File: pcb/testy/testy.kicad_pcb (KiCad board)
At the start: 2 copper layers, 116.4 x 88.4 mm, 21 parts, among them SW0:0 SW_Push, SW0:1 SW_Push, SW0:2 SW_Push, SW1:0 SW_Push, SW1:1 SW_Push, SW1:2 SW_Push, U1 ProMicro

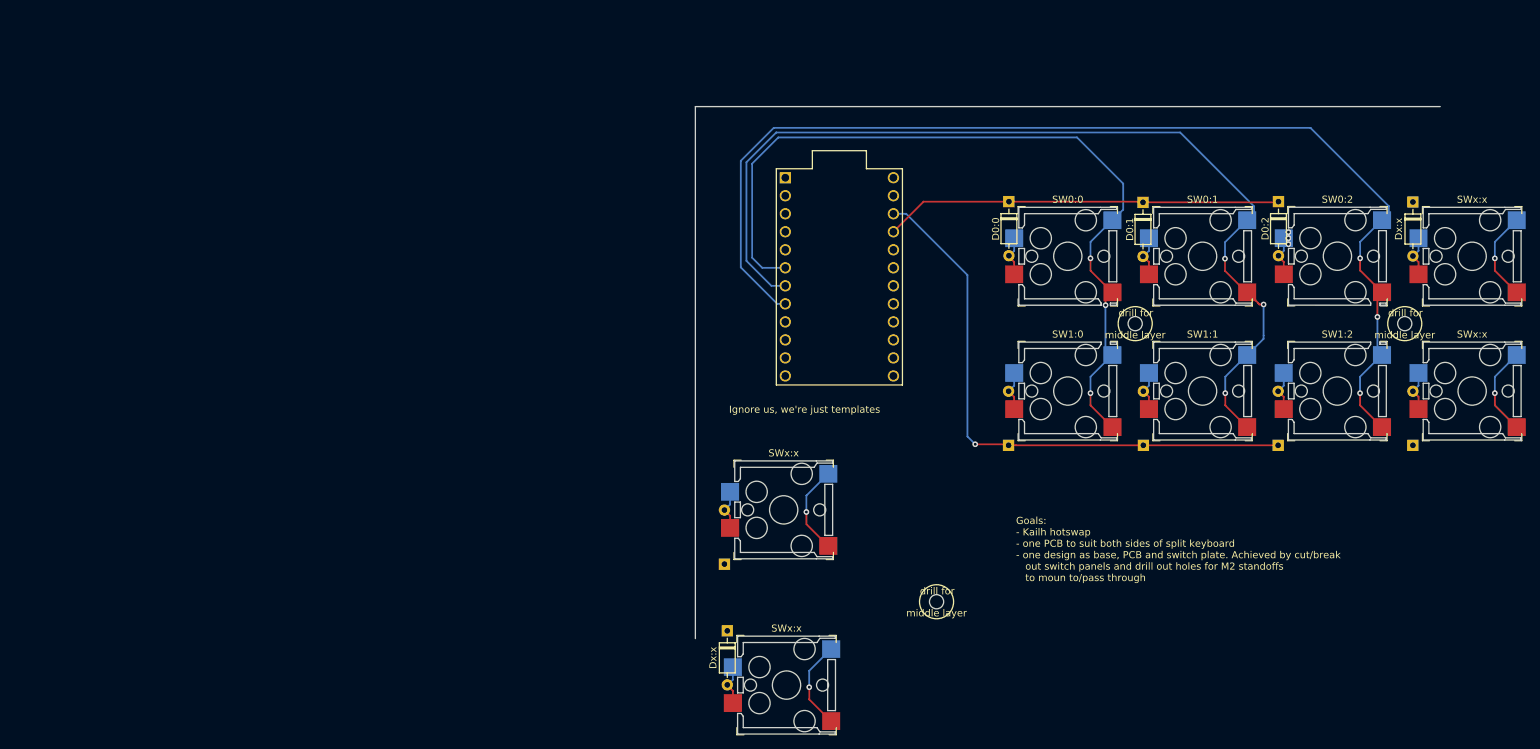
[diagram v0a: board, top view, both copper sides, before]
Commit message: feat: add reset switch and TRRS connector, test making promicro snapoff
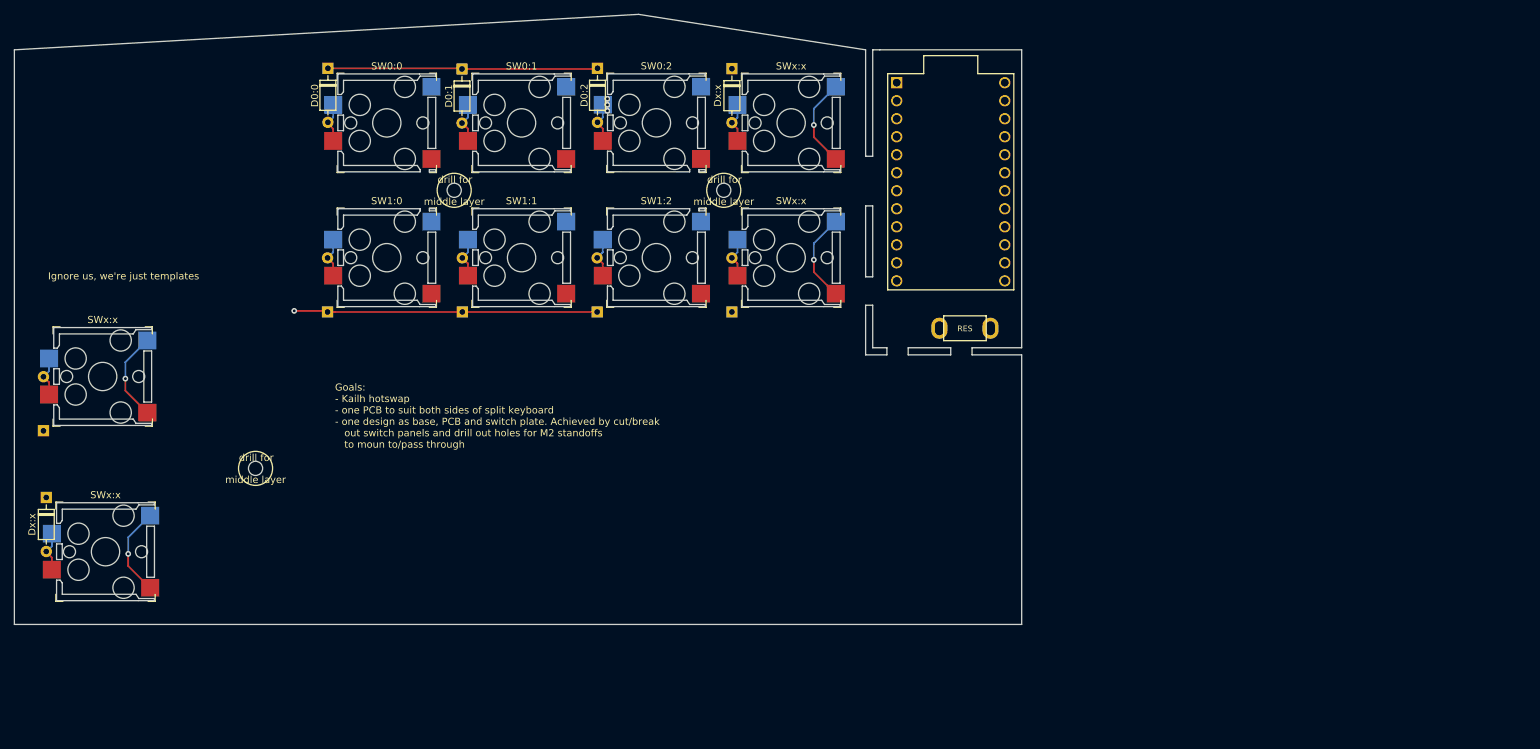
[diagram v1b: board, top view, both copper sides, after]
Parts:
- added RES1: SW_PUSH, footprints:TACT_SWITCH_TVBP06, F.Cu at (188.0, 83.0)
- moved D0:1 97.8 mm to (117.1, 44.7)
- moved D0:2 97.8 mm to (136.2, 44.6)
- moved D1:0 97.8 mm to (98.2, 79.0)
- moved D1:1 97.8 mm to (117.2, 79.0)
- moved D1:2 97.8 mm to (136.2, 79.0)
- moved Dx:x 97.8 mm to (155.2, 44.6)
- moved Dx:x 97.8 mm to (155.2, 79.0)
- moved Dx:x 97.8 mm to (58.5, 105.1)
- moved Dx:x 97.8 mm to (58.1, 95.7)
- moved SW0:0 97.8 mm to (106.5, 52.3)
- moved SW0:1 97.8 mm to (125.5, 52.3)
- moved SW0:2 97.8 mm to (144.5, 52.3)
- moved SW1:0 97.8 mm to (106.5, 71.3)
- moved SW1:1 97.8 mm to (125.5, 71.3)
- moved SW1:2 97.8 mm to (144.5, 71.3)
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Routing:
- net Col2: track 158.5 -> 0.00 mm, vias 3 -> 0
- net Col1: track 137.4 -> 0.00 mm, vias 3 -> 0
- net Col0: track 116.0 -> 0.00 mm, vias 3 -> 0
- net Row1: track 81.1 -> 42.8 mm
- net Row0: track 56.1 -> 38.1 mm
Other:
- board size 116.4 x 88.4 mm -> 142 x 86 mm

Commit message: feat: add all switches and LEDs to schematic
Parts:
- added Drill: MountingHole_2.2mm_M2_Pad_Via, MountingHole:MountingHole_2.2mm_M2_Pad_Via, F.Cu at (116.0, 61.8)
- added Drill: MountingHole_2.2mm_M2_Pad_Via, MountingHole:MountingHole_2.2mm_M2_Pad_Via, F.Cu at (154.0, 61.8)
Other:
- outline, holes or cut-outs redrawn
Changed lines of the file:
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@@
   (general
     (thickness 1.6)
-    (drawings 334)
+    (drawings 326)
     (tracks 81)
     (zones 0)
-    (modules 22)
+    (modules 24)
     (nets 31)
   )
@@
     (add_net Row1)
   )
+  (module MountingHole:MountingHole_2.2mm_M2_Pad_Via (layer F.Cu)
+    (at 116 61.8 270)
+    (descr "Mounting Hole 2.2mm, M2")
+    (tags "mounting hole 2.2mm m2")
+    (attr virtual)
+    (fp_text reference Drill (at 0 -3.2 90) (layer F.SilkS)
+      (effects (font (size 1 1) (thickness 0.15)))
+    )
+    (fp_text value MountingHole_2.2mm_M2_Pad_Via (at 0 3.2 90) (layer F.Fab)
+      (effects (font (size 1 1) (thickness 0.15)))
+    )
+    (fp_text user %R (at 0.3 0 90) (layer F.Fab)
+      (effects (font (size 1 1) (thickness 0.15)))
+    )
+    (fp_circle (center 0 0) (end 2.2 0) (layer Cmts.User) (width 0.15))
+    (fp_circle (center 0 0) (end 2.45 0) (layer F.CrtYd) (width 0.05))
+    (pad 1 thru_hole circle (at 0 0 270) (size 4.4 4.4) (drill 2.2) (layers *.Cu *.Mask))
+    (pad 1 thru_hole circle (at 1.65 0 270) (size 0.7 0.7) (drill 0.4) (layers *.Cu *.Mask))
+    (pad 1 thru_hole circle (at 1.166726 1.166726 270) (size 0.7 0.7) (drill 0.4) (layers *.Cu *.Mask))
+    (pad 1 thru_hole circle (at 0 1.65 270) (size 0.7 0.7) (drill 0.4) (layers *.Cu *.Mask))
+    (pad 1 thru_hole circle (at -1.166726 1.166726 270) (size 0.7 0.7) (drill 0.4) (layers *.Cu *.Mask))
+    (pad 1 thru_hole circle (at -1.65 0 270) (size 0.7 0.7) (drill 0.4) (layers *.Cu *.Mask))
+    (pad 1 thru_hole circle (at -1.166726 -1.166726 270) (size 0.7 0.7) (drill 0.4) (layers *.Cu *.Mask))
+    (pad 1 thru_hole circle (at 0 -1.65 270) (size 0.7 0.7) (drill 0.4) (layers *.Cu *.Mask))
+    (pad 1 thru_hole circle (at 1.166726 -1.166726 270) (size 0.7 0.7) (drill 0.4) (layers *.Cu *.Mask))
+  )
+  (module MountingHole:MountingHole_2.2mm_M2_Pad_Via (layer F.Cu)
+    (at 154 61.8 270)
+    (descr "Mounting Hole 2.2mm, M2")
+    (tags "mounting hole 2.2mm m2")
+    (attr virtual)
+    (fp_text reference Drill (at 0 -3.2 90) (layer F.SilkS)
+      (effects (font (size 1 1) (thickness 0.15)))
+    )
+    (fp_text value MountingHole_2.2mm_M2_Pad_Via (at 0 3.2 90) (layer F.Fab)
+      (effects (font (size 1 1) (thickness 0.15)))
+    )
+    (fp_circle (center 0 0) (end 2.45 0) (layer F.CrtYd) (width 0.05))
+    (fp_circle (center 0 0) (end 2.2 0) (layer Cmts.User) (width 0.15))
+    (fp_text user %R (at 0.3 0 90) (layer F.Fab)
+      (effects (font (size 1 1) (thickness 0.15)))
+    )
+    (pad 1 thru_hole circle (at 1.166726 -1.166726 270) (size 0.7 0.7) (drill 0.4) (layers *.Cu *.Mask))
+    (pad 1 thru_hole circle (at 0 -1.65 270) (size 0.7 0.7) (drill 0.4) (layers *.Cu *.Mask))
+    (pad 1 thru_hole circle (at -1.166726 -1.166726 270) (size 0.7 0.7) (drill 0.4) (layers *.Cu *.Mask))
+    (pad 1 thru_hole circle (at -1.65 0 270) (size 0.7 0.7) (drill 0.4) (layers *.Cu *.Mask))
+    (pad 1 thru_hole circle (at -1.166726 1.166726 270) (size 0.7 0.7) (drill 0.4) (layers *.Cu *.Mask))
+    (pad 1 thru_hole circle (at 0 1.65 270) (size 0.7 0.7) (drill 0.4) (layers *.Cu *.Mask))
+    (pad 1 thru_hole circle (at 1.166726 1.166726 270) (size 0.7 0.7) (drill 0.4) (layers *.Cu *.Mask))
+    (pad 1 thru_hole circle (at 1.65 0 270) (size 0.7 0.7) (drill 0.4) (layers *.Cu *.Mask))
+    (pad 1 thru_hole circle (at 0 0 270) (size 4.4 4.4) (drill 2.2) (layers *.Cu *.Mask))
+  )
   (module footprints:TACT_SWITCH_TVBP06 (layer F.Cu)
     (at 188 83)
@@
   (gr_line (start 176 42) (end 196 42) (layer Edge.Cuts) (width 0.05))
   (gr_line (start 174 42) (end 174 57) (layer Edge.Cuts) (width 0.05))
-  (gr_circle (center 154 61.8) (end 155 61.8) (layer Edge.Cuts) (width 0.05))
-  (gr_text "drill for" (at 154.1 60.3) (layer F.SilkS)
-    (effects (font (size 1 1) (thickness 0.15)))
-  )
-  (gr_text "middle layer" (at 154 63.4) (layer F.SilkS)
-    (effects (font (size 1 1) (thickness 0.15)))
-  )
-  (gr_circle (center 154 61.8) (end 156.4 61.8) (layer F.SilkS) (width 0.12))
   (gr_line (start 149.2 64.7) (end 149.2 64.4) (layer Edge.Cuts) (width 0.05))
   (gr_line (start 150.5 64.7) (end 151.4 64.7) (layer Edge.Cuts) (width 0.05))
@@
   (gr_line (start 112.5 64.7) (end 112.5 64.4) (layer Edge.Cuts) (width 0.05))
   (gr_line (start 113.4 64.7) (end 112.5 64.7) (layer Edge.Cuts) (width 0.05))
-  (gr_circle (center 116 61.8) (end 118.4 61.8) (layer F.SilkS) (width 0.12))
-  (gr_circle (center 116 61.8) (end 117 61.8) (layer Edge.Cuts) (width 0.05))
-  (gr_text "drill for" (at 116.1 60.3) (layer F.SilkS)
-    (effects (font (size 1 1) (thickness 0.15)))
-  )
-  (gr_text "middle layer" (at 116 63.4) (layer F.SilkS)
-    (effects (font (size 1 1) (thickness 0.15)))
-  )
   (gr_text "Goals:\n- Kailh hotswap\n- one PCB to suit both sides of split keyboard\n- one design as base, PCB and switch plate. Achieved by cut/break\n   out switch panels and drill out holes for M2 standoffs\n   to moun to/pass through" (at 99.2 93.6) (layer F.SilkS)
     (effects (font (size 1 1) (thickness 0.15)) (justify left))

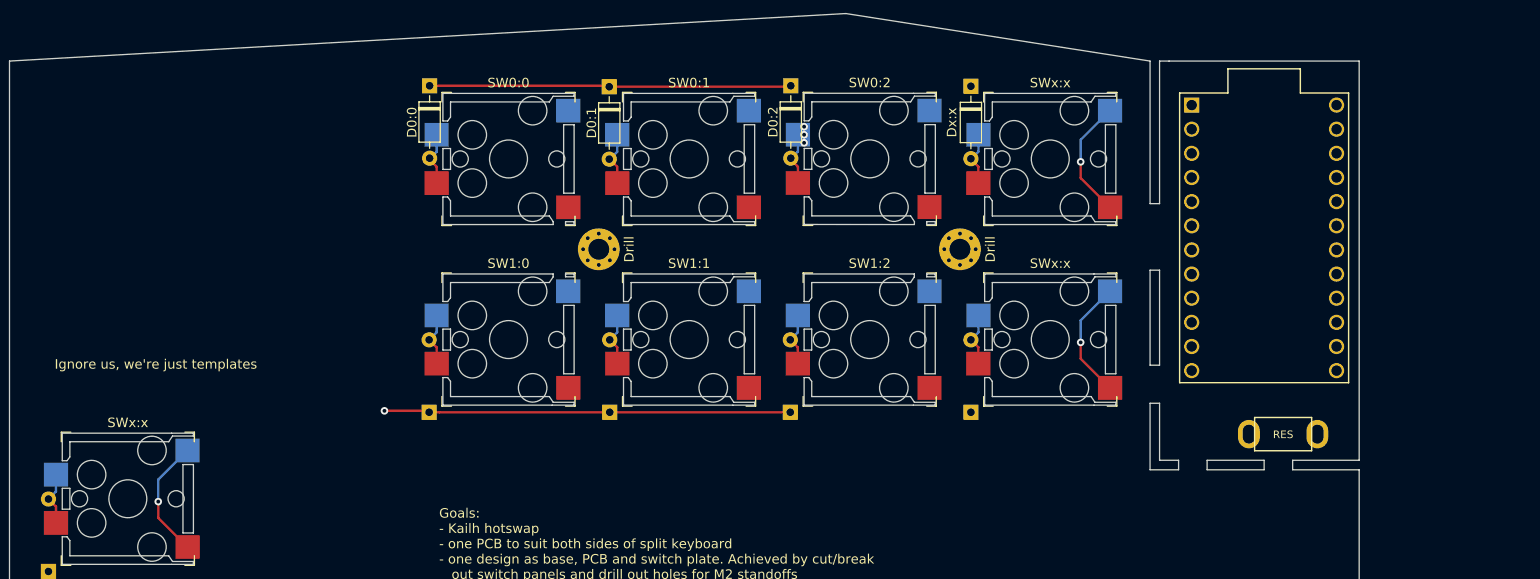
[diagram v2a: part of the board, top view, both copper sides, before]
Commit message: fix: get TRRS schematic to line up with footprint
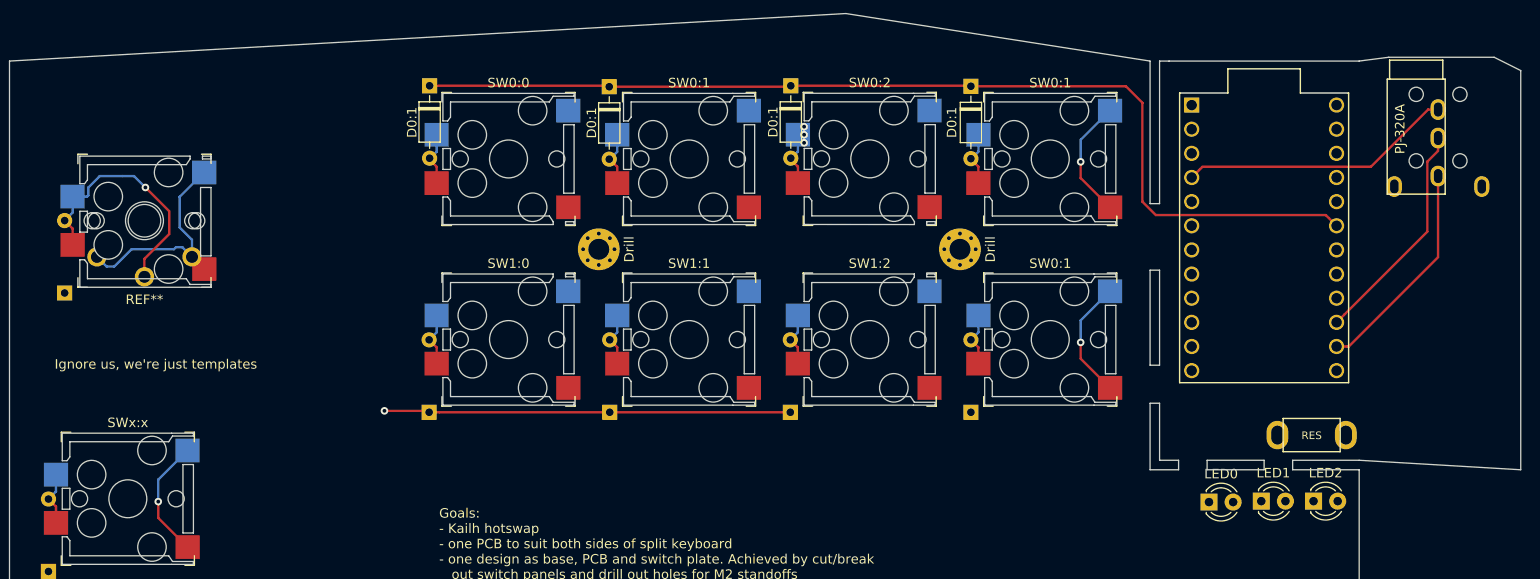
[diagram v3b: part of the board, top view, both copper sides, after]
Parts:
- removed RES1: SW_PUSH, footprints:TACT_SWITCH_TVBP06
- added Dx:x: 1N4148, Diode_THT:D_DO-35_SOD27_P7.62mm_Horizontal, B.Cu at (59.8, 66.4)
- added LED0: LED, footprints:LED_D3.0mm, F.Cu at (180.2, 88.4)
- added LED1: LED, LED_THT:LED_D3.0mm, F.Cu at (185.7, 88.3)
- added LED2: LED, LED_THT:LED_D3.0mm, F.Cu at (191.2, 88.3)
- added REF**: PG1511_socket, footprints:kailh-socket-and-choc-solder-reversible, F.Cu at (68.2, 58.8)
- added SW-reset1: SW_Push, footprints:TACT_SWITCH_TVBP06, F.Cu at (191.0, 83.1)
- added TRRS1: MJ-4PP-9, footprints:TRRS-PJ-320A-dual, F.Cu at (204.3, 43.9)
- renumbered Dx:x to D0:1, D1:2 to D0:1, D1:1 to D0:1, D1:0 to D0:1, D0:0 to D0:1, D0:2 to D0:1, SWx:x to SW0:1
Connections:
- net Net-(U1-Pad10) renamed Col5
- net Net-(U1-Pad11) renamed Col6
- net Net-(U1-Pad23) renamed Row4
- net Net-(U1-Pad9) renamed Col4
- D0:1 pad 1: (no net) -> Row0 (x2)
- D0:1 pad 2: (no net) -> Net-(D0:1-Pad2) (x2)
- D0:1 pad 1: Row1 -> Row0 (x3)
- D0:1 pad 2: Net-(D1:2-Pad2) -> Net-(D0:1-Pad2)
- D0:1 pad 2: Net-(D1:1-Pad2) -> Net-(D0:1-Pad2)
- D0:1 pad 2: Net-(D1:0-Pad2) -> Net-(D0:1-Pad2)
- D0:1 pad 2: Net-(D0:0-Pad2) -> Net-(D0:1-Pad2)
- D0:1 pad 2: Net-(D0:2-Pad2) -> Net-(D0:1-Pad2)
- SW0:1 pad 1: (no net) -> Col1 (x2)
- SW0:1 pad 2: (no net) -> Net-(D0:1-Pad2) (x2)
- U1 pad 12: Net-(U1-Pad12) -> LED2
- U1 pad 14: Net-(U1-Pad14) -> data
- U1 pad 15: Net-(U1-Pad15) -> GND
- U1 pad 16: Net-(U1-Pad16) -> GND
- U1 pad 18: Net-(U1-Pad18) -> LED0
- U1 pad 19: Net-(U1-Pad19) -> Row0
- U1 pad 2: Net-(U1-Pad2) -> GND
- U1 pad 20: Net-(U1-Pad20) -> Row1
- U1 pad 21: Row0 -> Row2
- U1 pad 22: Row1 -> Row3
- U1 pad 24: Net-(U1-Pad24) -> LED1
- U1 pad 3: Net-(U1-Pad3) -> Reset
- U1 pad 4: Net-(U1-Pad4) -> VCC
- U1 pad 5: Net-(U1-Pad5) -> Col0
- U1 pad 6: Col0 -> Col1
- U1 pad 7: Col1 -> Col2
- U1 pad 8: Col2 -> Col3
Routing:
- net Row0: track 38.1 -> 150.5 mm, vias 0 -> 1
- net Row1: track 42.8 -> 0.00 mm, vias 1 -> 0
- net VCC: track 0.00 -> 28.9 mm
- net Col1: track 0.00 -> 25.5 mm, vias 0 -> 2
- net GND: track 0.00 -> 23.8 mm
- net data: track 0.00 -> 23.1 mm
- net (no net): track 73.9 -> 87.7 mm, vias 4 -> 3
- net Net-(D0:1-Pad2): track 5.73 -> 17.2 mm
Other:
- board size 142 x 86 mm -> 159 x 86 mm

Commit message: feat: more playing with layout
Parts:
- added Dx:x: 1N4148, Diode_THT:D_DO-35_SOD27_P7.62mm_Horizontal, B.Cu at (155.2, 41.0)
- added Dx:x: 1N4148, Diode_THT:D_DO-35_SOD27_P7.62mm_Horizontal, F.Cu at (189.2, 101.7)
- added Dx:x: 1N4148, Diode_THT:D_DO-35_SOD27_P7.62mm_Horizontal, F.Cu at (174.2, 82.7)
- added Dx:x: 1N4148, Diode_THT:D_DO-35_SOD27_P7.62mm_Horizontal, F.Cu at (155.2, 82.7)
- added SWx:x: SW_Push, footprints:Kailh_socket_reversible, F.Cu at (163.5, 33.3)
- added SWx:x: SW_Push, footprints:Kailh_socket_reversible, F.Cu at (197.5, 109.3)
- added SWx:x: SW_Push, footprints:Kailh_socket_reversible, F.Cu at (182.5, 90.3)
- added SWx:x: SW_Push, footprints:Kailh_socket_reversible, F.Cu at (163.5, 90.3)
- moved TRRS1 21.2 mm to (196.0, 63.4), turned to 270 degrees
- moved U1 19.3 mm to (188.0, 41.4)
- moved LED0 18.3 mm to (196.4, 97.0), turned to 90 degrees
- moved SW-reset1 12.2 mm to (187.1, 71.5), turned to 180 degrees
- moved LED1 11.1 mm to (196.3, 91.5), turned to 90 degrees
- moved LED2 5.59 mm to (196.3, 86.0), turned to 90 degrees
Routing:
- net (no net): track 87.7 -> 161.6 mm, vias 3 -> 7
- net VCC: track 28.9 -> 0.00 mm
- net GND: track 23.8 -> 0.00 mm
- net data: track 23.1 -> 0.00 mm
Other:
- board size 159 x 86 mm -> 155.3 x 101.9 mm
- board text added: "<--- Should we have centered holes to make drilling easier?"
